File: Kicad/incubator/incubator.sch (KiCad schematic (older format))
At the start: 20 parts, among them J1 Barrel_Jack_MountingPin, J2 Conn_01x06, J3 Conn_01x01, J4 RJ12, J5 Conn_01x01, J6 Conn_01x01, J7 Conn_01x01

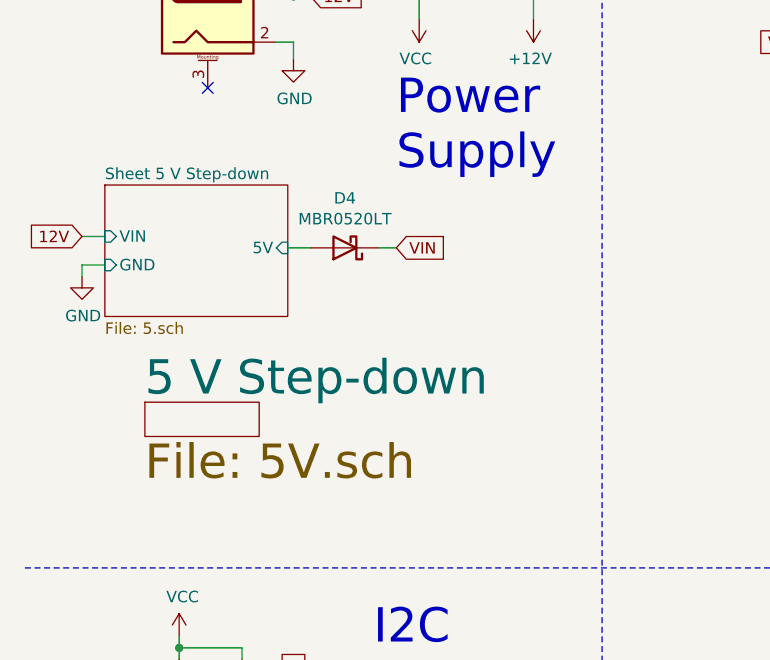
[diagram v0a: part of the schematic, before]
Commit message: refactor:Step-down IC was changed
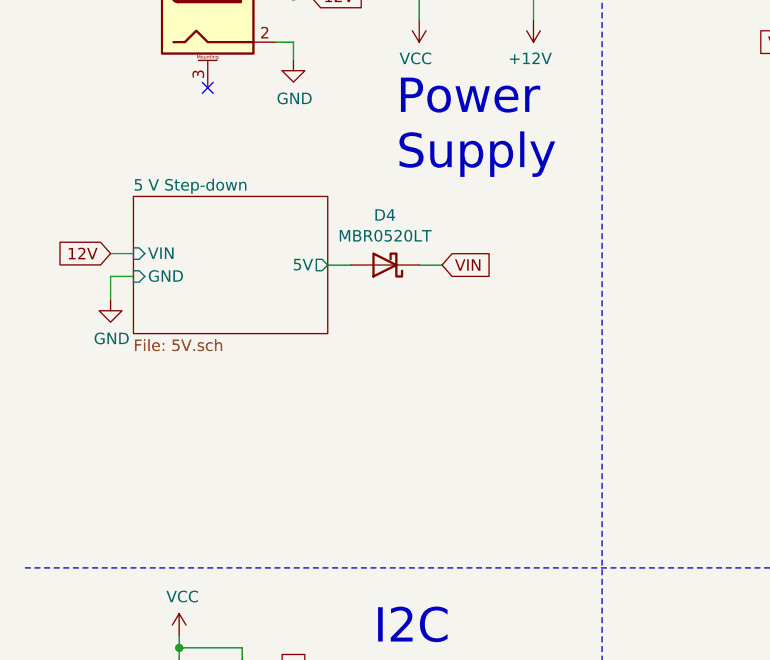
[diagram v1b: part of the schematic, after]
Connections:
- net Sheet 5 V Step-down/5V renamed 5 V Step-down/5V
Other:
- moved on the sheet: D4
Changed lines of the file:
@@
 $Descr A4 11693 8268
 encoding utf-8
-Sheet 1 5
+Sheet 1 4
 Title "Incubator"
 Date "2021-07-26"
@@
 Wire Wire Line
 	2700 925  2700 775
-Wire Wire Line
-	1625 1925 1725 1925
-$Sheet
-S 825  1650 800  575
-U 61054A11
-F0 "Sheet 5 V Step-down" 50
-F1 "5.sch" 50
-F2 "VIN" I L 825 1875 50
-F3 "GND" I L 825 2000 50
-F4 "5V" I R 1625 1925 50
-$EndSheet
-Wire Wire Line
-	725  2000 725  2050
-Wire Wire Line
-	825  2000 725  2000
 $Comp
 L incubator-rescue:GND-power #PWR0109
 U 1 1 61068D10
-P 725 2050
-F 0 "#PWR0109" H 725 1800 50  0001 C CNN
-F 1 "GND" H 730 1877 50  0000 C CNN
-F 2 "" H 725 2050 50  0001 C CNN
-F 3 "" H 725 2050 50  0001 C CNN
-	1    725  2050
-	1    0    0    -1
-$EndComp
-Wire Wire Line
-	825  1875 725  1875
-Text GLabel 725  1875 0    50   Input ~ 0
+P 850 2150
+F 0 "#PWR0109" H 850 1900 50  0001 C CNN
+F 1 "GND" H 855 1977 50  0000 C CNN
+F 2 "" H 850 2150 50  0001 C CNN
+F 3 "" H 850 2150 50  0001 C CNN
+	1    850  2150
+	1    0    0    -1
+$EndComp
+Text GLabel 850  1950 0    50   Input ~ 0
 12V
 Wire Wire Line
@@
 	1    0    0    -1
 $EndComp
-Text GLabel 2100 1925 2    50   Input ~ 0
+Text GLabel 2300 2000 2    50   Input ~ 0
 VIN
 Text GLabel 8050 3325 2    50   Input ~ 0
@@
 L incubator-rescue:MBR0520LT-Diode D4
 U 1 1 61137931
-P 1875 1925
-F 0 "D4" H 1875 1708 50  0000 C CNN
-F 1 "MBR0520LT" H 1875 1799 50  0000 C CNN
-F 2 "Diode_SMD:D_SOD-123" H 1875 1750 50  0001 C CNN
-F 3 "http://www.onsemi.com/pub_link/Collateral/MBR0520LT1-D.PDF" H 1875 1925 50  0001 C CNN
-	1    1875 1925
+P 2050 2000
+F 0 "D4" H 2050 1783 50  0000 C CNN
+F 1 "MBR0520LT" H 2050 1874 50  0000 C CNN
+F 2 "Diode_SMD:D_SOD-123" H 2050 1825 50  0001 C CNN
+F 3 "http://www.onsemi.com/pub_link/Collateral/MBR0520LT1-D.PDF" H 2050 2000 50  0001 C CNN
+	1    2050 2000
 	-1   0    0    1
 $EndComp
-Wire Wire Line
-	2100 1925 2025 1925
 $Comp
 L incubator-rescue:C-Device C?
@@
 $EndComp
 $Sheet
-S 1000 2600 500  150
+S 950  1700 850  600
 U 614262A1
-F0 "5 V Step-down" 150
-F1 "5V.sch" 150
+F0 "5 V Step-down" 50
+F1 "5V.sch" 50
+F2 "VIN" I L 950 1950 50
+F3 "5V" O R 1800 2000 50
+F4 "GND" I L 950 2050 50
 $EndSheet
+Wire Wire Line
+	850  2150 850  2050
+Wire Wire Line
+	850  2050 950  2050
+Wire Wire Line
+	850  1950 950  1950
+Wire Wire Line
+	2300 2000 2200 2000
+Wire Wire Line
+	1900 2000 1800 2000
 $EndSCHEMATC

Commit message: refactor: final test version
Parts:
- removed H5, H6, H7, H8: MountingHole, MountingHole:MountingHole_4.5mm, symbol incubator-rescue:MountingHole-Mechanical
- added C1: 0.33u, Capacitor_SMD:C_0805_2012Metric_Pad1.18x1.45mm_HandSolder, symbol incubator-rescue:C-Device
- added C2: 100n, Capacitor_SMD:C_0805_2012Metric_Pad1.18x1.45mm_HandSolder, symbol incubator-rescue:C-Device
- added D1, D2: GREEN, LED_SMD:LED_0805_2012Metric_Pad1.15x1.40mm_HandSolder, symbol Device:LED
- added D3: MBR0520LT, Diode_SMD:D_SOD-123, symbol incubator-rescue:MBR0520LT-Diode
- added J8: Conn_02x03_Odd_Even, Connector:Tag-Connect_TC2030-IDC-NL_2x03_P1.27mm_Vertical, symbol Connector_Generic:Conn_02x03_Odd_Even
- added R3: 10k, Resistor_SMD:R_0805_2012Metric_Pad1.20x1.40mm_HandSolder, symbol Device:R
- added R4: 1k, Resistor_SMD:R_0805_2012Metric_Pad1.20x1.40mm_HandSolder, symbol Device:R
- added U1: LM78M05_TO252, Package_TO_SOT_SMD:TO-252-2, symbol Regulator_Linear:LM78M05_TO252
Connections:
- net +12V: now also C1.1, R3.1, U1.1 (VI)
- net GND: now also C1.2, C2.2, D1.1 (K), D2.1 (K), J8.6 (Pin_6), U1.2 (GND)
- net MISO: now also J8.1 (Pin_1)
- net MOSI: now also J8.4 (Pin_4)
- net SCK: now also J8.3 (Pin_3)
- net VIN: now also D3.1 (K), R4.1
- net ~RESET: now also J8.5 (Pin_5)
- net 5 V Step-down/5V: no longer names the net of D4.2 (A)
- net 5 V Step-down/5V: now also C2.1, U1.3 (VO)
- new net: D1.2 (A), R3.2
- new net: D2.2 (A), R4.2
- new net: D3.2 (A), J8.2 (Pin_2)
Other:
- note added: "Power LEDS"
- note removed: "FAN HOLES"
- moved on the sheet: D4
